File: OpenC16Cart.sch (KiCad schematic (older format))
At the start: 14 parts, among them CN1 C16_EXP_PORT_44PIN, J1 Conn_02x03_Odd_Even, J2 Conn_02x03_Odd_Even, SW1 BTN_RESET, U1 27512

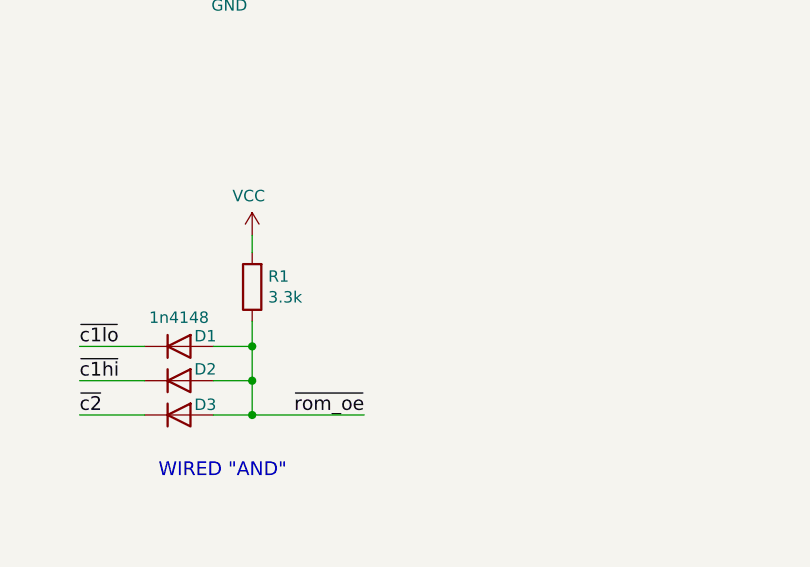
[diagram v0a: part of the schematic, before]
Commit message: Fix R1 value and A14/15 labels
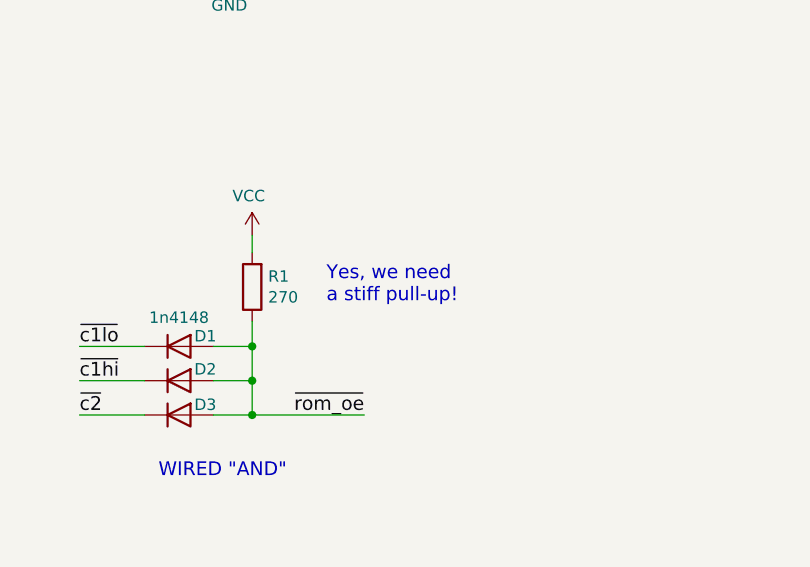
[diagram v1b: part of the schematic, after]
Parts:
- R1: value 3.3k -> 270
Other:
- note added: "Yes, we need\na stiff pull-up!"
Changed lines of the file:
@@
 P 5490 5120
 F 0 "R1" H 5420 5074 50  0000 R CNN
-F 1 "3.3k" H 5420 5165 50  0000 R CNN
+F 1 "270" H 5420 5165 50  0000 R CNN
 F 2 "Resistor_THT:R_Axial_DIN0204_L3.6mm_D1.6mm_P7.62mm_Horizontal" V 5420 5120 50  0001 C CNN
 F 3 "~" H 5490 5120 50  0001 C CNN
@@
 Wire Bus Line
 	4390 1655 4390 2955
+Text Notes 5815 5195 0    60   ~ 0
+Yes, we need\na stiff pull-up!
 $EndSCHEMATC

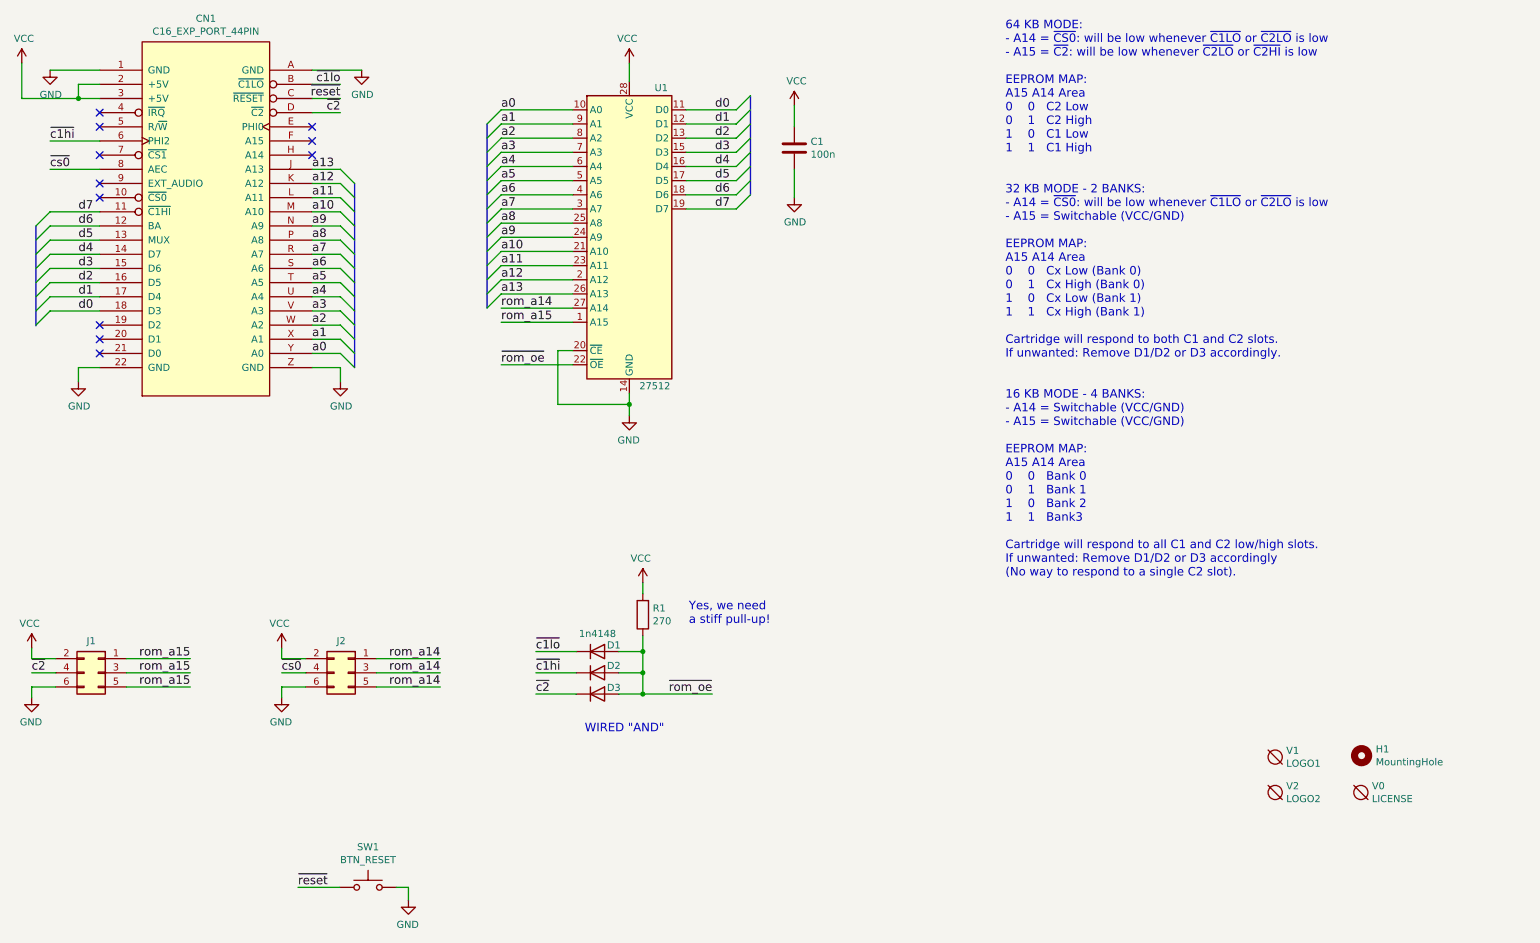
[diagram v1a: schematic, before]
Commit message: Switch to new pinout
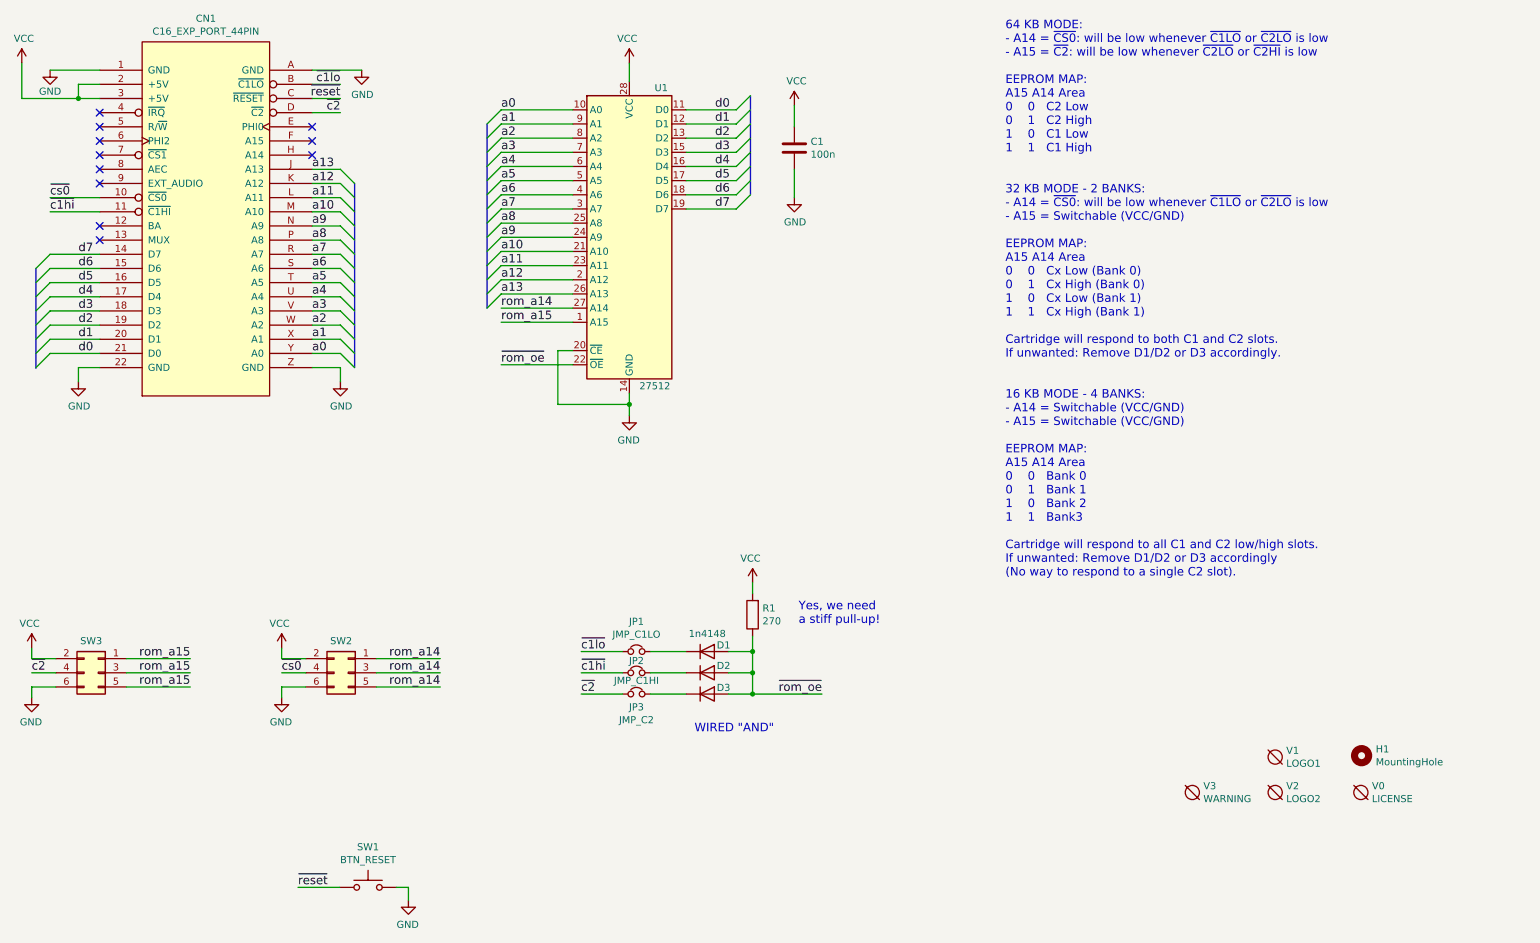
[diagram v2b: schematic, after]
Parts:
- added JP1: JMP_C1LO, Jumper:SolderJumper-2_P1.3mm_Bridged_RoundedPad1.0x1.5mm, symbol Device:Jumper_NC_Small
- added JP2: JMP_C1HI, Jumper:SolderJumper-2_P1.3mm_Bridged_RoundedPad1.0x1.5mm, symbol Device:Jumper_NC_Small
- added JP3: JMP_C2, Jumper:SolderJumper-2_P1.3mm_Bridged_RoundedPad1.0x1.5mm, symbol Device:Jumper_NC_Small
- added V3: WARNING, w_logo:Logo_silk_warning_10x8.5mm, symbol void:Void
- renumbered J2 to SW2, J1 to SW3
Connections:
- net d0: now also CN1.21 (D0); no longer CN1.18 (D3)
- net d1: now also CN1.20 (D1); no longer CN1.17 (D4)
- net d2: now also CN1.19 (D2); no longer CN1.16 (D5)
- net d3: now also CN1.18 (D3); no longer CN1.15 (D6)
- net d4: now also CN1.17 (D4); no longer CN1.14 (D7)
- net d5: now also CN1.16 (D5); no longer CN1.13 (MUX)
- net d6: now also CN1.15 (D6); no longer CN1.12 (BA)
- net d7: now also CN1.14 (D7); no longer CN1.11 (~C1HI)
- net ~c1hi: now also CN1.11 (~C1HI), JP2.1; no longer CN1.6 (PHI2), D2.1 (K)
- net ~c1lo: now also JP1.1; no longer D1.1 (K)
- net ~c2: now also JP3.1; no longer D3.1 (K)
- net ~cs0: now also CN1.10 (~CS0); no longer CN1.8 (AEC)
- new net: D1.1 (K), JP1.2
- new net: D2.1 (K), JP2.2
- new net: D3.1 (K), JP3.2
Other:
- moved on the sheet: D1, D2, D3, R1

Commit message: Ready for V5
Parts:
- R1: value 270 -> 1k
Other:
- note removed: "Yes, we need\na stiff pull-up!"
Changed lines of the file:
@@
 Sheet 1 1
 Title "Open Commodore 16/Plus4 Cartridge"
-Date "2023-10-03"
+Date "2026-03-09"
 Rev "5git"
 Comp "SukkoPera"
@@
 P 6265 5120
 F 0 "R1" H 6195 5074 50  0000 R CNN
-F 1 "270" H 6195 5165 50  0000 R CNN
+F 1 "1k" H 6195 5165 50  0000 R CNN
 F 2 "Resistor_THT:R_Axial_DIN0204_L3.6mm_D1.6mm_P7.62mm_Horizontal" V 6195 5120 50  0001 C CNN
 F 3 "~" H 6265 5120 50  0001 C CNN
@@
 WIRED "AND"
 Text Notes 8050 4860 0    60   ~ 0
-64 KB MODE:\n- A14 = ~CS0~: will be low whenever ~C1LO~ or ~C2LO~ is low\n- A15 = ~C2~: will be low whenever ~C2LO~ or ~C2HI~ is low\n\nEEPROM MAP:\nA15 A14 Area\n0    0   C2 Low\n0    1   C2 High\n1    0   C1 Low\n1    1   C1 High\n\n\n32 KB MODE - 2 BANKS:\n- A14 = ~CS0~: will be low whenever ~C1LO~ or ~C2LO~ is low\n- A15 = Switchable (VCC/GND)\n\nEEPROM MAP:\nA15 A14 Area\n0    0   Cx Low (Bank 0)\n0    1   Cx High (Bank 0)\n1    0   Cx Low (Bank 1)\n1    1   Cx High (Bank 1)\n\nCartridge will respond to both C1 and C2 slots.\nIf unwanted: Remove D1/D2 or D3 accordingly.\n\n\n16 KB MODE - 4 BANKS:\n- A14 = Switchable (VCC/GND)\n- A15 = Switchable (VCC/GND)\n\nEEPROM MAP:\nA15 A14 Area\n0    0   Bank 0\n0    1   Bank 1\n1    0   Bank 2\n1    1   Bank3\n\nCartridge will respond to all C1 and C2 low/high slots.\nIf unwanted: Remove D1/D2 or D3 accordingly\n(No way to respond to a single C2 slot).
+64 KB MODE:\n- A14 = ~CS0~: will be low whenever ~C1LO~ or ~C2LO~ is low\n- A15 = ~C2~: will be low whenever ~C2LO~ or ~C2HI~ is low\n\nEEPROM MAP:\nA15 A14 Area\n0    0   C2 Low\n0    1   C2 High\n1    0   C1 Low\n1    1   C1 High\n\n\n32 KB MODE - 2 BANKS:\n- A14 = ~CS0~: will be low whenever ~C1LO~ or ~C2LO~ is low\n- A15 = Switchable (VCC/GND)\n\nEEPROM MAP:\nA15 A14 Area\n0    0   Cx Low (Bank 0)\n0    1   Cx High (Bank 0)\n1    0   Cx Low (Bank 1)\n1    1   Cx High (Bank 1)\n\nCartridge will respond to both C1 and C2 slots.\nIf unwanted: Remove D1/D2 or D3 accordingly.\n\n\n16 KB MODE - 4 BANKS:\n- A14 = Switchable (VCC/GND)\n- A15 = Switchable (VCC/GND)\n\nEEPROM MAP:\nA15 A14 Area\n0    0   Bank 0\n0    1   Bank 1\n1    0   Bank 2\n1    1   Bank 3\n\nCartridge will respond to all C1 and C2 low/high slots.\nIf unwanted: Remove D1/D2 or D3 accordingly\n(No way to respond to a single C2 slot).
 Text Label 5055 5530 0    60   ~ 0
 ~c1hi
@@
 Wire Wire Line
 	3350 7045 3055 7045
-Text Notes 6590 5195 0    60   ~ 0
-Yes, we need\na stiff pull-up!
 NoConn ~ 1655 2375
 NoConn ~ 1655 2475
@@
 	-1   0    0    -1
 $EndComp
+$Comp
+L void:Void V3
+U 1 1 667AE1F4
+P 9370 6375
+F 0 "V3" H 9448 6421 50  0000 L CNN
+F 1 "WARNING" H 9448 6330 50  0000 L CNN
+F 2 "w_logo:Logo_silk_warning_10x8.5mm" H 9370 6375 50  0001 C CNN
+F 3 "" H 9370 6375 50  0001 C CNN
+	1    9370 6375
+	1    0    0    -1
+$EndComp
 Wire Bus Line
 	6250 1455 6250 2155
@@
 Wire Bus Line
 	4390 1655 4390 2955
-$Comp
-L void:Void V3
-U 1 1 667AE1F4
-P 9370 6375
-F 0 "V3" H 9448 6421 50  0000 L CNN
-F 1 "WARNING" H 9448 6330 50  0000 L CNN
-F 2 "w_logo:Logo_silk_warning_10x8.5mm" H 9370 6375 50  0001 C CNN
-F 3 "" H 9370 6375 50  0001 C CNN
-	1    9370 6375
-	1    0    0    -1
-$EndComp
 $EndSCHEMATC
